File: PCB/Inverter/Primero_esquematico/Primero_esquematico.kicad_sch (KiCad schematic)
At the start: 0 parts

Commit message: Correcciones incompletas e instalaciones de un par de extensiones copadas
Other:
- added sheet LogicSupply (LogicSupply.kicad_sch)
- sheet Gate_Driver ports: added none; removed 15V
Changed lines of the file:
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@@
 (kicad_sch
-	(version 20231120)
+	(version 20260306)
 	(generator "eeschema")
-	(generator_version "8.0")
+	(generator_version "10.0")
 	(paper "A4")
+	(wire
+		(pts
+			(xy 212.09 97.79) (xy 215.9 97.79)
+		)
+		(stroke
+			(width 0)
+			(type default)
+		)
+	)
+	(symbol
+		(lib_id "power:+12V")
+		(at 212.09 97.79 0)
+		(unit 1)
+		(body_style 1)
+		(exclude_from_sim no)
+		(in_bom yes)
+		(on_board yes)
+		(in_pos_files yes)
+		(dnp no)
+		(fields_autoplaced yes)
+		(property "Reference" "#PWR02"
+			(at 212.09 101.6 0)
+			(hide yes)
+			(show_name no)
+			(do_not_autoplace no)
+			(effects
+				(font
+					(size 1.27 1.27)
+				)
+			)
+		)
+		(property "Value" "+12V"
+			(at 212.09 92.71 0)
+			(show_name no)
+			(do_not_autoplace no)
+			(effects
+				(font
+					(size 1.27 1.27)
+				)
+			)
+		)
+		(property "Footprint" ""
+			(at 212.09 97.79 0)
+			(hide yes)
+			(show_name no)
+			(do_not_autoplace no)
+			(effects
+				(font
+					(size 1.27 1.27)
+				)
+			)
+		)
+		(property "Datasheet" ""
+			(at 212.09 97.79 0)
+			(hide yes)
+			(show_name no)
+			(do_not_autoplace no)
+			(effects
+				(font
+					(size 1.27 1.27)
+				)
+			)
+		)
+		(property "Description" "Power symbol creates a global label with name \"+12V\""
+			(at 212.09 97.79 0)
+			(hide yes)
+			(show_name no)
+			(do_not_autoplace no)
+			(effects
+				(font
+					(size 1.27 1.27)
+				)
+			)
+		)
+		(pin "1"
+		)
+		(instances
+			(project "Primero_esquematico"
+				(path "/d930f486-f6ac-489c-907e-47f2cb34cf04"
+					(reference "#PWR02")
+					(unit 1)
+				)
+			)
+		)
+	)
 	(sheet
-		(at 213.36 60.96)
-		(size 15.24 16.51)
+		(at 215.9 92.71)
+		(size 15.24 13.97)
+		(exclude_from_sim no)
+		(in_bom yes)
+		(on_board yes)
+		(dnp no)
 		(fields_autoplaced yes)
 		(stroke
@@
 		)
 		(fill
-			(color 0 0 0 0.0000)
+			(color 0 0 0 0)
+		)
+		(property "Sheetname" "LogicSupply"
+			(at 215.9 91.9984 0)
+			(show_name no)
+			(do_not_autoplace no)
+			(effects
+				(font
+					(size 1.27 1.27)
+				)
+				(justify left bottom)
+			)
+		)
+		(property "Sheetfile" "LogicSupply.kicad_sch"
+			(at 215.9 107.2646 0)
+			(show_name no)
+			(do_not_autoplace no)
+			(effects
+				(font
+					(size 1.27 1.27)
+				)
+				(justify left top)
+			)
+		)
+		(pin "Vin_FB" input
+			(at 215.9 97.79 180)
+			(effects
+				(font
+					(size 1.27 1.27)
+				)
+				(justify left)
+			)
+		)
+		(instances
+			(project "Primero_esquematico"
+				(path "/d930f486-f6ac-489c-907e-47f2cb34cf04"
+					(page "10")
+				)
+			)
+		)
+	)
+	(sheet
+		(at 213.36 60.96)
+		(size 15.24 16.51)
+		(exclude_from_sim no)
+		(in_bom yes)
+		(on_board yes)
+		(dnp no)
+		(fields_autoplaced yes)
+		(stroke
+			(width 0.1524)
+			(type solid)
+		)
+		(fill
+			(color 0 0 0 0)
 		)
 		(property "Sheetname" "currentS"
 			(at 213.36 60.2484 0)
+			(show_name no)
+			(do_not_autoplace no)
 			(effects
 				(font
@@
 		(property "Sheetfile" "currentS.kicad_sch"
 			(at 213.36 78.0546 0)
+			(show_name no)
+			(do_not_autoplace no)
 			(effects
 				(font
@@
 		(at 58.42 43.18)
 		(size 36.83 48.26)
+		(exclude_from_sim no)
+		(in_bom yes)
+		(on_board yes)
+		(dnp no)
 		(fields_autoplaced yes)
 		(stroke
@@
 		)
 		(fill
-			(color 0 0 0 0.0000)
+			(color 0 0 0 0)
 		)
 		(property "Sheetname" "Gate_Driver"
 			(at 58.42 42.4684 0)
+			(show_name no)
+			(do_not_autoplace no)
 			(effects
 				(font
@@
 		(property "Sheetfile" "g_driver.kicad_sch"
 			(at 58.42 92.0246 0)
+			(show_name no)
+			(do_not_autoplace no)
 			(effects
 				(font
@@
 				)
 				(justify left top)
-			)
-		)
-		(pin "15V" input
-			(at 95.25 46.99 0)
-			(effects
-				(font
-					(size 1.27 1.27)
-				)
-				(justify right)
 			)
 		)
@@
 		(at 134.62 54.61)
 		(size 27.94 34.29)
+		(exclude_from_sim no)
+		(in_bom yes)
+		(on_board yes)
+		(dnp no)
 		(fields_autoplaced yes)
 		(stroke
@@
 		)
 		(fill
-			(color 0 0 0 0.0000)
+			(color 0 0 0 0)
 		)
 		(property "Sheetname" "Core"
 			(at 134.62 53.8984 0)
+			(show_name no)
+			(do_not_autoplace no)
 			(effects
 				(font
@@
 		(property "Sheetfile" "core.kicad_sch"
 			(at 134.62 89.4846 0)
+			(show_name no)
+			(do_not_autoplace no)
 			(effects
 				(font
@@
 		)
 	)
+	(embedded_fonts no)
 )

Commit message: Termine el circuito de corriente
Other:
- sheet currentS ports: added none; removed 15V
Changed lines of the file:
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@@
 	)
 	(sheet
-		(at 213.36 60.96)
+		(at 213.36 62.23)
 		(size 15.24 16.51)
 		(exclude_from_sim no)
@@
 		)
 		(property "Sheetname" "currentS"
-			(at 213.36 60.2484 0)
+			(at 213.36 61.5184 0)
 			(show_name no)
 			(do_not_autoplace no)
@@
 		)
 		(property "Sheetfile" "currentS.kicad_sch"
-			(at 213.36 78.0546 0)
+			(at 213.36 79.3246 0)
 			(show_name no)
 			(do_not_autoplace no)
@@
 			)
 		)
-		(pin "15V" input
-			(at 213.36 64.77 180)
-			(effects
-				(font
-					(size 1.27 1.27)
-				)
-				(justify left)
-			)
-		)
 		(pin "Uot1" input
-			(at 213.36 68.58 180)
+			(at 213.36 66.04 180)
 			(effects
 				(font
@@
 		)
 		(pin "Uot2" input
-			(at 213.36 71.12 180)
+			(at 213.36 69.85 180)
 			(effects
 				(font

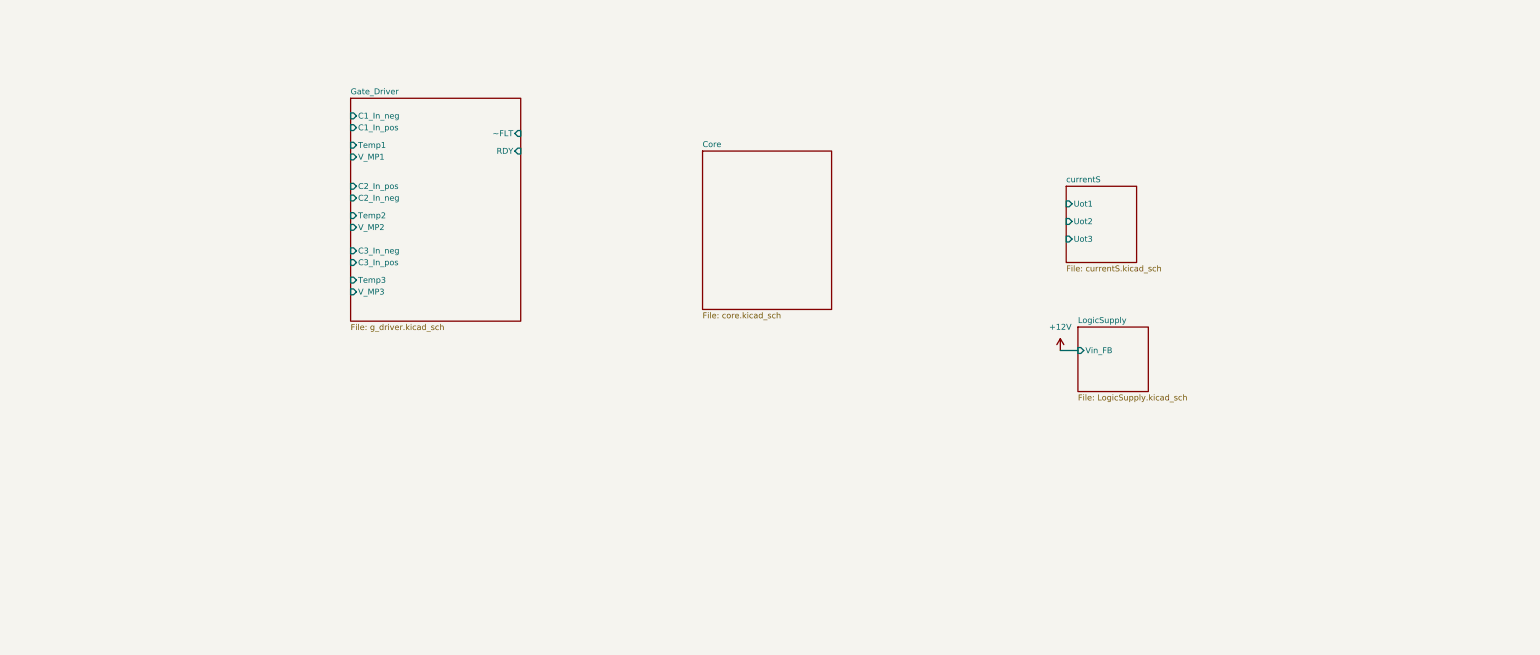
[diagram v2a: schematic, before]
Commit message: Coloque filtros y sensores
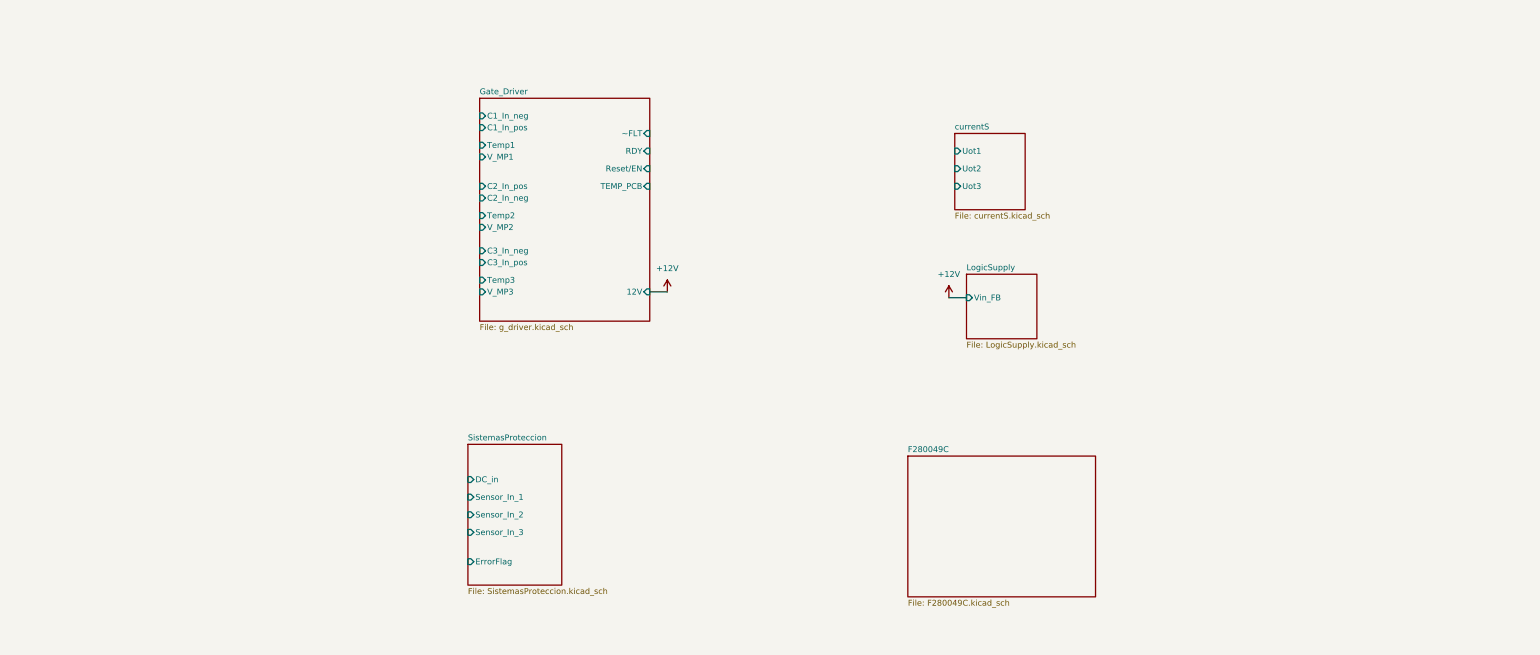
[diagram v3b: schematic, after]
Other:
- removed sheet Core
- added sheet F280049C (F280049C.kicad_sch)
- added sheet SistemasProteccion (SistemasProteccion.kicad_sch)
- sheet Gate_Driver ports: added 12V, Reset/EN, TEMP_PCB; removed none

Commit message: Esquematico practicamente terminado
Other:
- removed sheet F280049C
- removed sheet Gate_Driver
- removed sheet LogicSupply
- removed sheet SistemasProteccion
- removed sheet currentS
- added sheet pcb_logica (pcb_logica.kicad_sch)
- added sheet pcb_potencia (pcb_potencia.kicad_sch)
- note added: "Falta cambar los conectores Molex q se pusieron por los Molex Mini 50"
- note added: "Falta terminar de colocar esto pero se hara cuando se tengan todos los componentes situados en la pcb para ver de que forma es mas comodo de poner y cuantos se necesite"

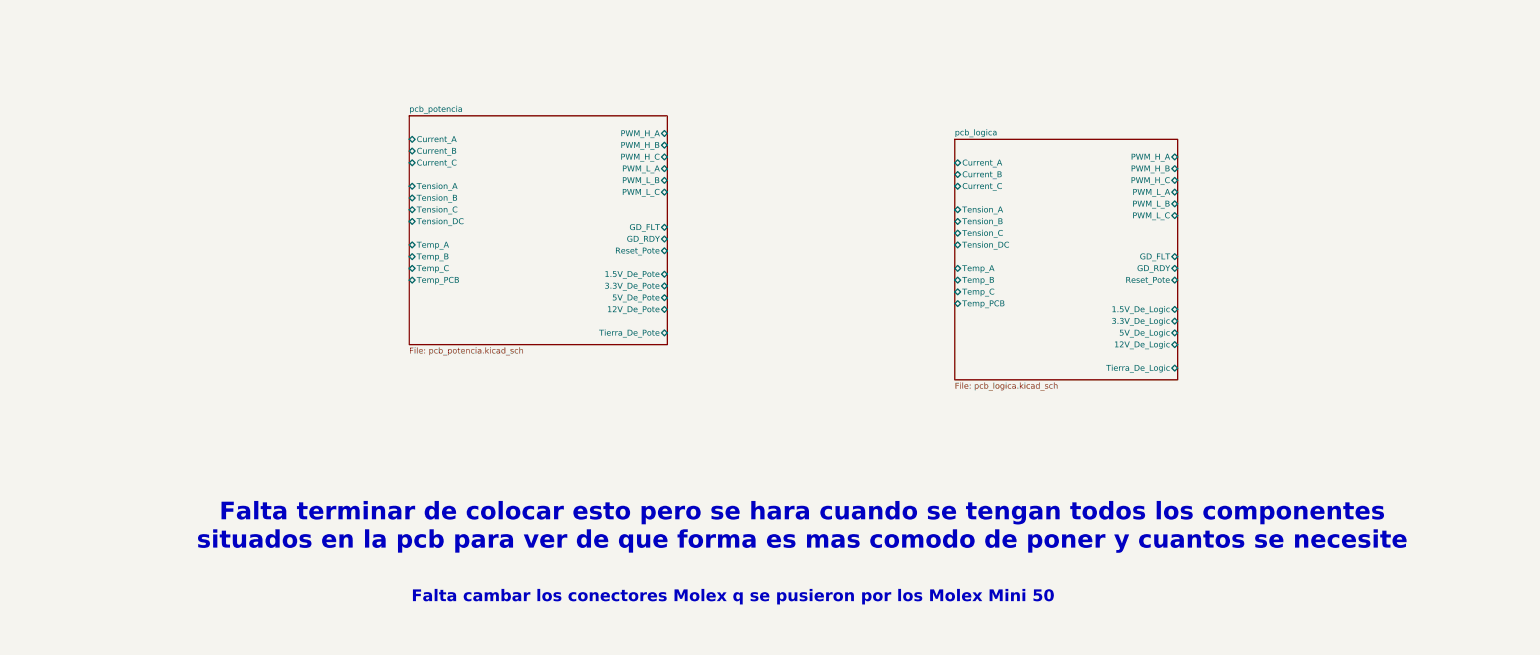
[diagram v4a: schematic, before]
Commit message: Un par de cosas q corregi del ERC pero sigue mal
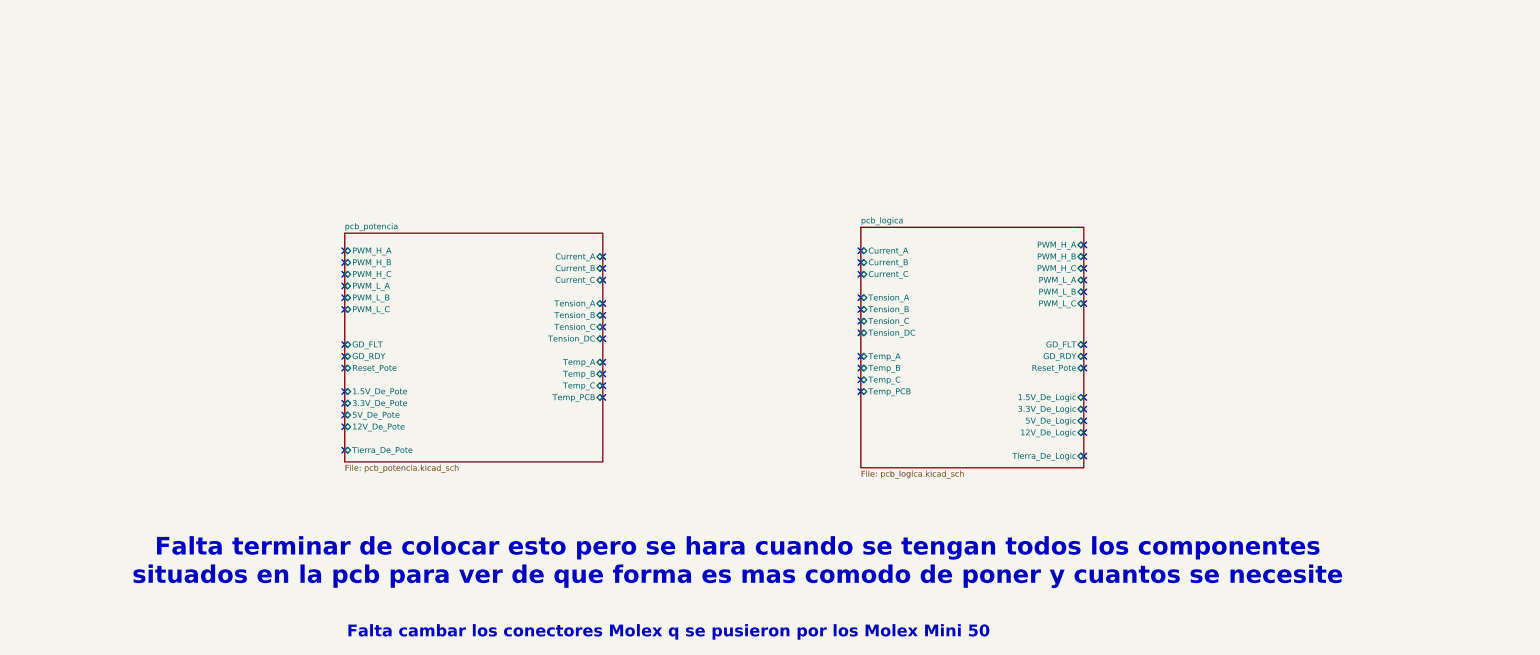
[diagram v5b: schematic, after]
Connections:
- no-connect marks 0 -> 50

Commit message: Algunos cambios
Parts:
- added C178: 220uF, Snapeda:WCAP-PSLC_8X11.7_DXL_, symbol Snapeda:WCAP-PSLC_8X11.7
- added D75: SMDJ13A, Diode_SMD:D_SMC, symbol Device:D_TVS
- added J3: 349128023, Snapeda:CONN_SD-34912-001_02_MOL, symbol Snapeda:349128023
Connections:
- new net +12V: C178.1, D75.1 (A1), J3.1
- new net GND: C178.2, D75.2 (A2), J3.2, J3.MNT1, J3.MNT2
- no-connect marks 50 -> 0
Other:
- note added: "Chequear si este capa nos sirve o si tengo q poner una mas grande"
